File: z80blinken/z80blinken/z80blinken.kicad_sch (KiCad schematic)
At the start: 22 parts, among them J1 RCBus-80, J2 ADDR, J3 CTRL, J4 DATA, J5 A16_A23, J7 USER, SW1 RESET, U1 Z80CPU

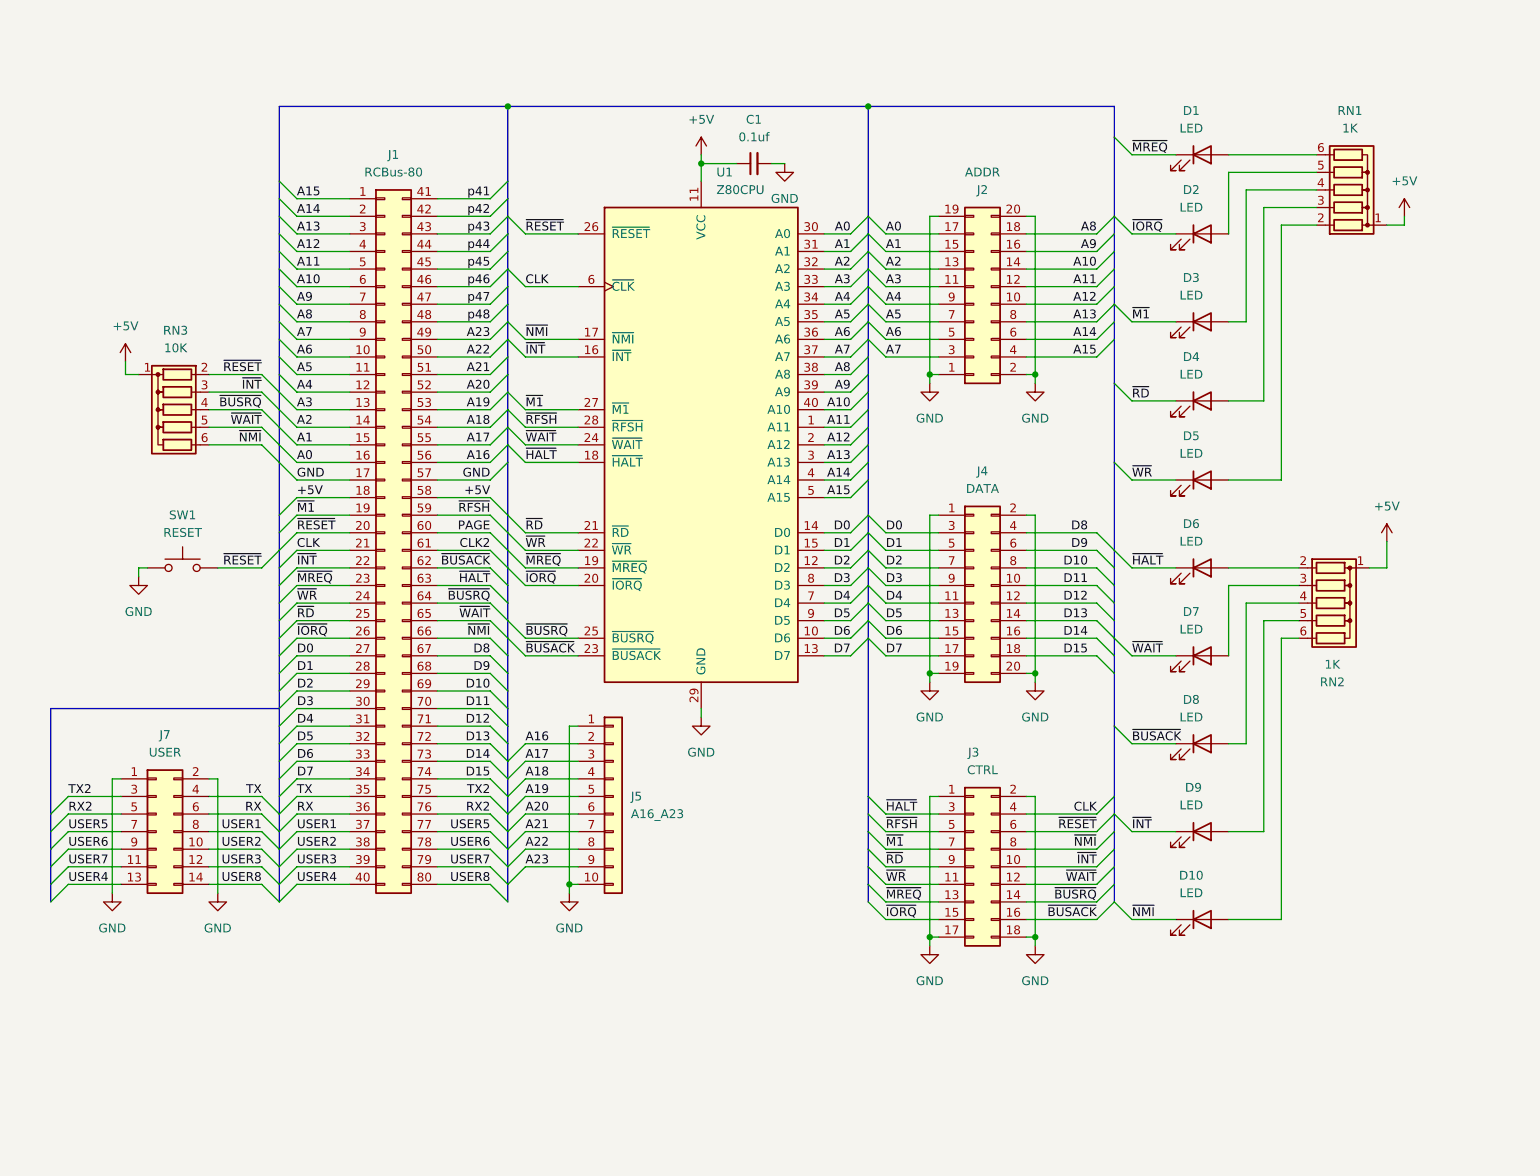
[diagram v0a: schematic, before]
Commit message: Remove test points; finish silkscreen
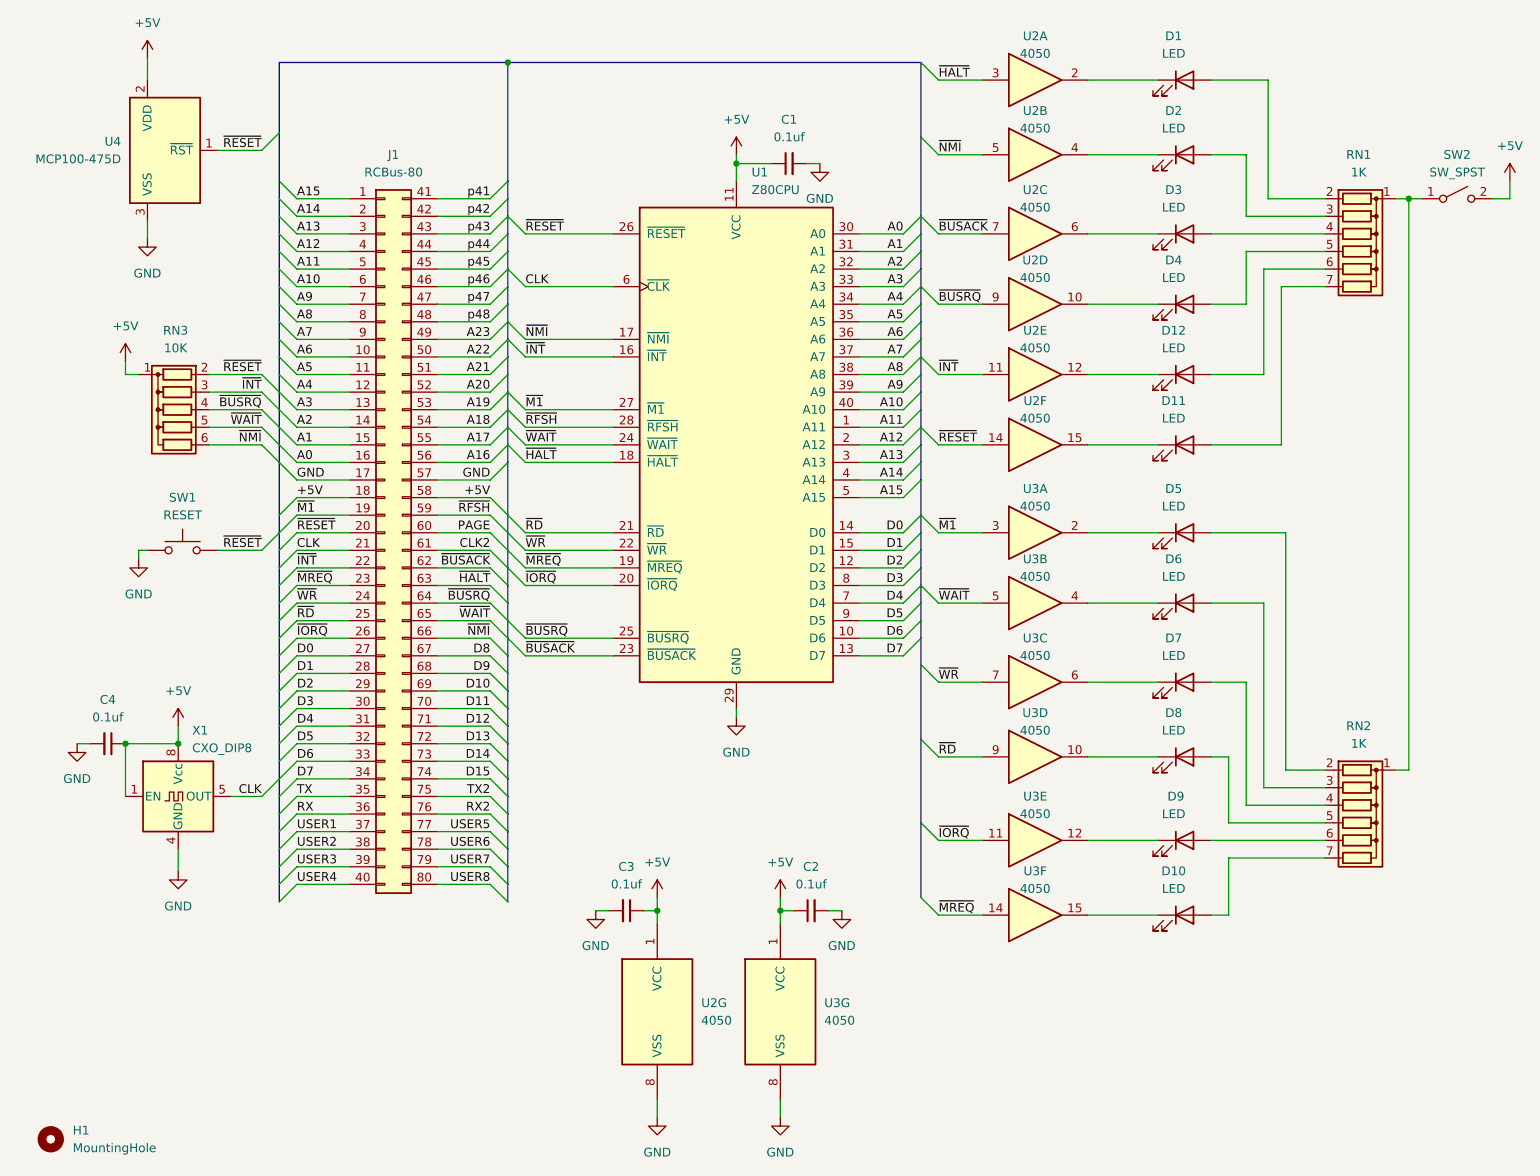
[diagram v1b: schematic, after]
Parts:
- removed J2: ADDR, Connector_PinHeader_2.54mm:PinHeader_2x10_P2.54mm_Horizontal, symbol Connector_Generic:Conn_02x10_Odd_Even
- removed J3: CTRL, Connector_PinHeader_2.54mm:PinHeader_2x09_P2.54mm_Horizontal, symbol Connector_Generic:Conn_02x09_Odd_Even
- removed J4: DATA, Connector_PinHeader_2.54mm:PinHeader_2x10_P2.54mm_Horizontal, symbol Connector_Generic:Conn_02x10_Odd_Even
- removed J5: A16_A23, Connector_PinHeader_2.54mm:PinHeader_1x10_P2.54mm_Vertical, symbol Connector_Generic:Conn_01x10
- removed J7: USER, Connector_PinHeader_2.54mm:PinHeader_2x07_P2.54mm_Horizontal, symbol Connector_Generic:Conn_02x07_Odd_Even
- removed RN1, RN2: 1K, Resistor_THT:R_Array_SIP6, symbol Device:R_Network05
- added C2, C3, C4: 0.1uf, Capacitor_THT:C_Disc_D3.0mm_W1.6mm_P2.50mm, symbol Device:C_Small
- added D11, D12: LED, Custom:LED_WP934CB&slash_GD_KNB, symbol Device:LED
- added H1: MountingHole, MountingHole:MountingHole_3.2mm_M3, symbol Mechanical:MountingHole
- added RN1, RN2: 1K, Resistor_THT:R_Array_SIP7, symbol Device:R_Network06
- added SW2: SW_SPST, SamacSys_Parts:JS202011CQN, symbol Switch:SW_SPST
- added U2, U3: 4050, Package_DIP:DIP-16_W7.62mm, symbol 4xxx:4050
- added U4: MCP100-475D, Package_TO_SOT_THT:TO-92_Inline, symbol Power_Supervisor:MCP100-475D
- added X1: CXO_DIP8, Oscillator:Oscillator_DIP-8, symbol Oscillator:CXO_DIP8
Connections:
- net +5V: now also C2.1, C3.1, C4.1, SW2.2 (B), U2.1 (VCC), U3.1 (VCC), U4.2 (VDD), X1.1 (EN), X1.8 (Vcc)
- net CLK: now also X1.5 (OUT)
- net GND: now also C2.2, C3.2, C4.2, U2.8 (VSS), U3.8 (VSS), U4.3 (VSS), X1.4 (GND)
- net ~{BUSACK}: now also U2.7; no longer D8.1 (K)
- net ~{BUSRQ}: now also U2.9
- net ~{HALT}: now also U2.3; no longer D6.1 (K)
- net ~{INT}: now also U2.11; no longer D9.1 (K)
- net ~{IORQ}: now also U3.11; no longer D2.1 (K)
- net ~{M1}: now also U3.3; no longer D3.1 (K)
- net ~{MREQ}: now also U3.14; no longer D1.1 (K)
- net ~{NMI}: now also U2.5; no longer D10.1 (K)
- net ~{RD}: now also U3.9; no longer D4.1 (K)
- net ~{RESET}: now also U2.14, U4.1 (~{RST})
- net ~{WAIT}: now also U3.5; no longer D7.1 (K)
- net ~{WR}: now also U3.7; no longer D5.1 (K)
- net at D2.2 (A): now also RN1.3 (R2)
- net at D9.2 (A): now also RN2.6 (R5)
- net at D3.2 (A): now also RN1.4 (R3)
- net at D6.2 (A): now also RN2.3 (R2)
- net at D1.2 (A): now also RN1.2 (R1)
- net at D5.2 (A): now also RN2.2 (R1)
- net at D4.2 (A): now also RN1.5 (R4)
- net at D7.2 (A): now also RN2.4 (R3)
- net at D8.2 (A): now also RN2.5 (R4)
- net at D10.2 (A): now also RN2.7 (R6)
- new net: D1.1 (K), U2.2
- new net: D12.1 (K), U2.12
- new net: D12.2 (A), RN1.6 (R5)
- new net: D2.1 (K), U2.4
- new net: D11.1 (K), U2.15
- new net: D11.2 (A), RN1.7 (R6)
- new net: D9.1 (K), U3.12
- new net: D10.1 (K), U3.15
- new net: D7.1 (K), U3.6
- new net: D6.1 (K), U3.4
- new net: D3.1 (K), U2.6
- new net: D5.1 (K), U3.2
- new net: RN1.1 (common), RN2.1 (common), SW2.1 (A)
- new net: D4.1 (K), U2.10
- new net: D8.1 (K), U3.10
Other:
- company: (none) -> (C) 2024 J.B. Langston
- title: (none) -> z80blinken
- moved on the sheet: C1, D1, D10, D2, D3, D4, D5, D6, D7, D8, D9, SW1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
